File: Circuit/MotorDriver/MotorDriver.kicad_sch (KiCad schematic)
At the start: 28 parts, among them J1 Conn_01x06_Pin, J2 USB_C_Receptacle_USB2.0_16P, SW1 SW_SPDT, SW2 SW_Push_Dual, U1 STM32G473RCTx, U2 CH340E, Y1 24M

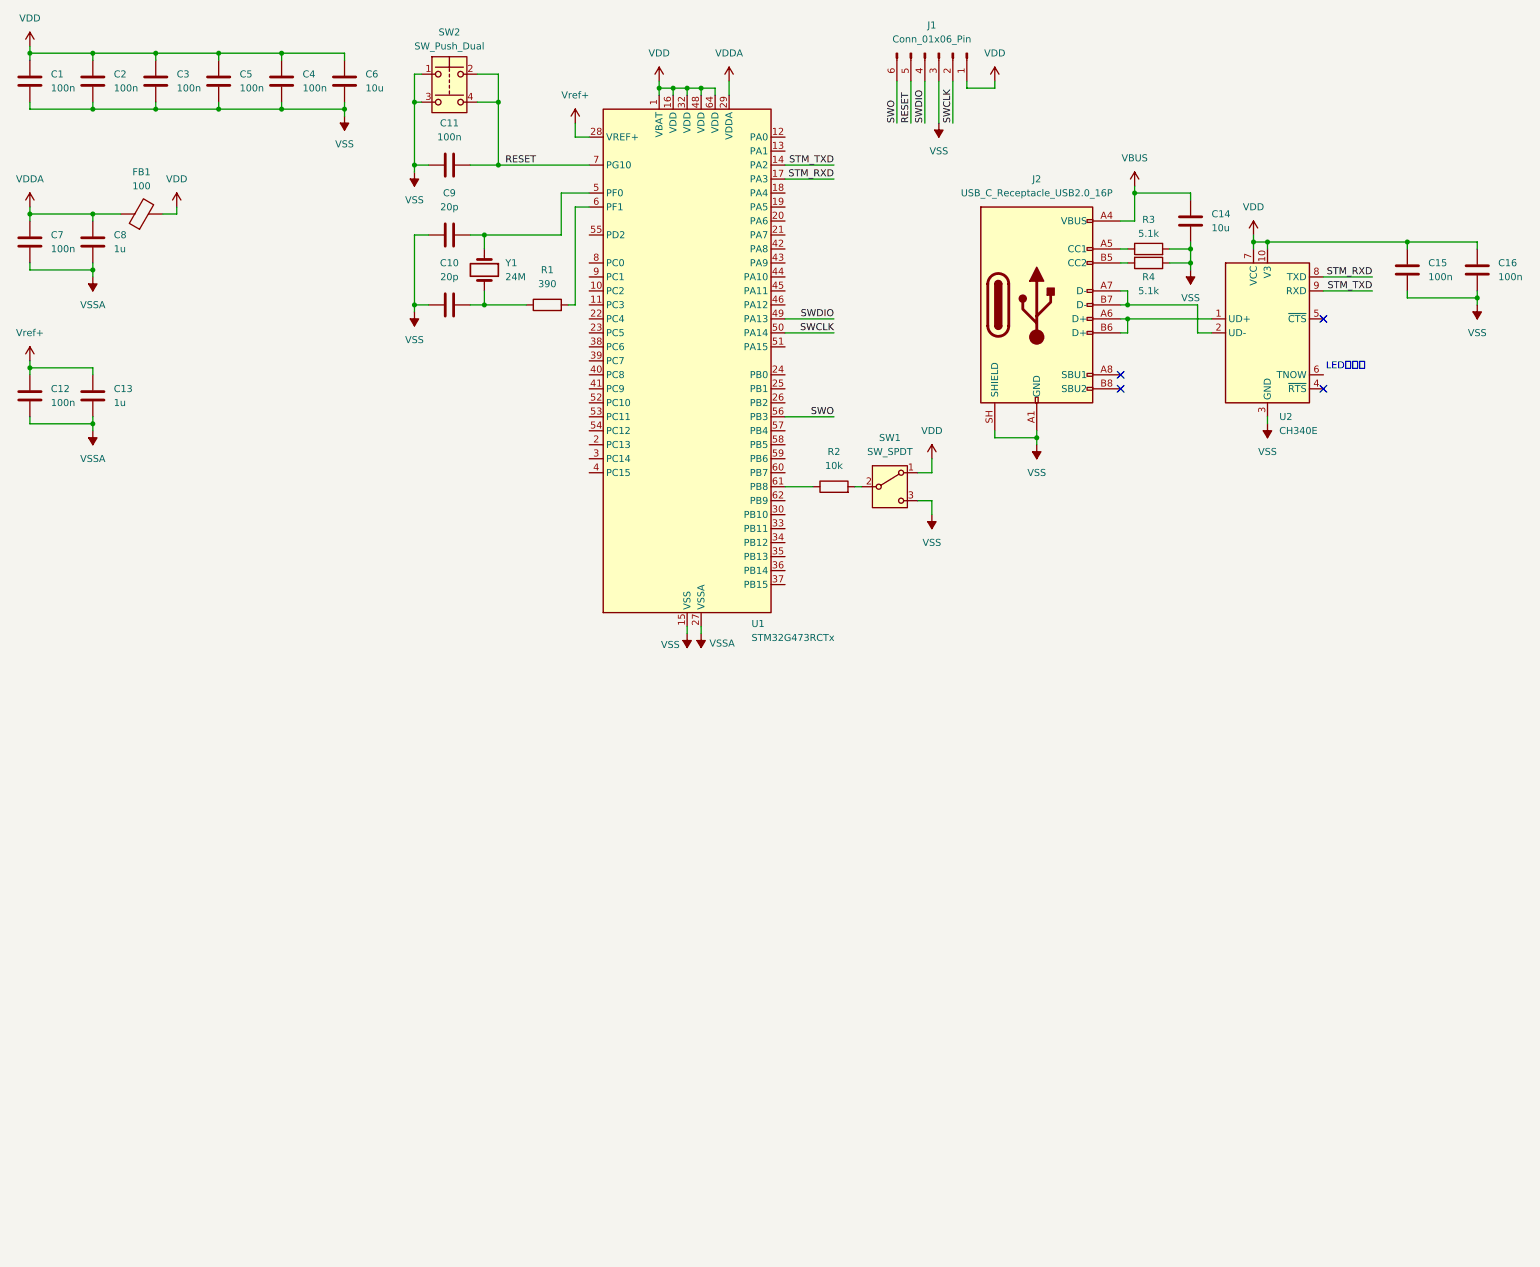
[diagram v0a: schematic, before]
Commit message: ドライバのシンボルを追加
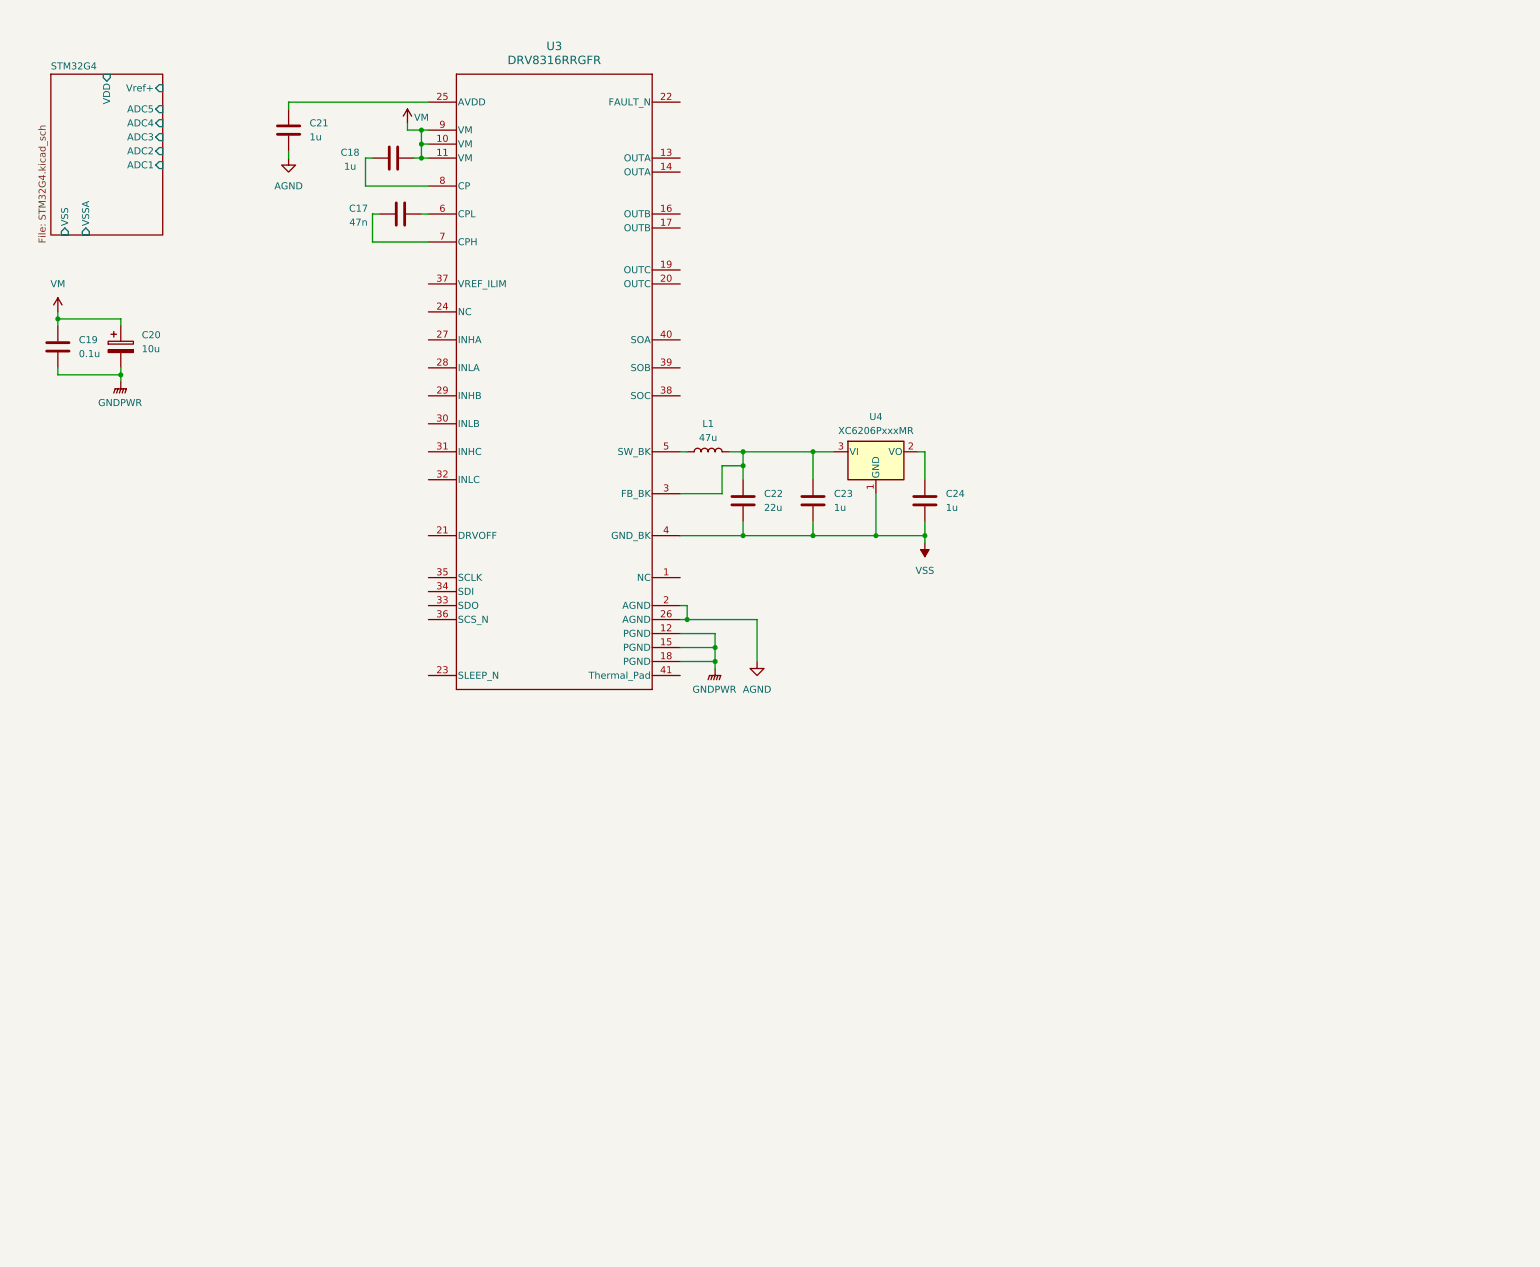
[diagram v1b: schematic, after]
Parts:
- removed C1, C11, C12, C15, C16, C2, C3, C4, C5, C7: 100n, symbol Device:C
- removed C10, C9: 20p, symbol Device:C
- removed C13, C8: 1u, symbol Device:C
- removed C14, C6: 10u, symbol Device:C
- removed FB1: 100, symbol Device:FerriteBead
- removed J1: Conn_01x06_Pin, symbol Connector:Conn_01x06_Pin
- removed J2: USB_C_Receptacle_USB2.0_16P, symbol Connector:USB_C_Receptacle_USB2.0_16P
- removed R1: 390, symbol Device:R
- removed R2: 10k, symbol Device:R
- removed R3, R4: 5.1k, symbol Device:R
- removed SW1: SW_SPDT, symbol Switch:SW_SPDT
- removed SW2: SW_Push_Dual, symbol Switch:SW_Push_Dual
- removed U1: STM32G473RCTx, Package_QFP:LQFP-64_10x10mm_P0.5mm, symbol MCU_ST_STM32G4:STM32G473RCTx
- removed U2: CH340E, Package_SO:MSOP-10_3x3mm_P0.5mm, symbol Interface_USB:CH340E
- removed Y1: 24M, symbol Device:Crystal
- added C17: 47n, symbol Device:C
- added C18, C21, C23, C24: 1u, symbol Device:C
- added C19: 0.1u, symbol Device:C
- added C20: 10u, symbol Device:C_Polarized
- added C22: 22u, symbol Device:C
- added L1: 47u, symbol Device:L
- added U3: DRV8316RRGFR, RGF0040E-IPC_A, symbol OU_power:DRV8316RRGFR
- added U4: XC6206PxxxMR, Package_TO_SOT_SMD:SOT-23-3, symbol Regulator_Linear:XC6206PxxxMR
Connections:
- net VSS: now also C22.2, C23.2, C24.2, U3.4 (GND_BK), U4.1 (GND)
- new net: C22.1, C23.1, L1.2, U3.3 (FB_BK), U4.3 (VI)
- new net: C24.1, U4.2 (VO)
- new net: L1.1, U3.5 (SW_BK)
- new net: C17.1, U3.6 (CPL)
- new net: C17.2, U3.7 (CPH)
- new net: C21.1, U3.25 (AVDD)
- new net: C18.1, U3.8 (CP)
- new net AGND: C21.2, U3.2 (AGND), U3.26 (AGND)
- new net GNDPWR: C19.2, C20.2, U3.12 (PGND), U3.15 (PGND), U3.18 (PGND)
- new net VM: C18.2, C19.1, C20.1, U3.10 (VM), U3.11 (VM), U3.9 (VM)
- no-connect marks 4 -> 0
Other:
- added sheet STM32G4 (STM32G4.kicad_sch)
- note removed: "LEDを接続"

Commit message: PWMとADCの配線等
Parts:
- added C25, C26: 30p, symbol Device:C
- added D1: BZT52C3V3, symbol Device:D_Zener
- added J3: Conn_01x03_Pin, symbol Connector:Conn_01x03_Pin
- added R5: 47k, symbol Device:R
- added R6: 5.1k, symbol Device:R
- added R7, R8: 1k, symbol Device:R
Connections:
- net VSS is gone; now on net AGND: C22.2, C23.2, C24.2, U3.4 (GND_BK), U4.1 (GND)
- net AGND: now also U3.41 (Thermal_Pad), C25.2, C26.2, D1.2 (A)
- net STM32G4/ADC1: now also C25.1, R7.1
- net STM32G4/ADC2: now also C26.1, R8.1
- net VM: now also R5.1
- net VDD: now reaches C24.1, U4.2 (VO)
- net VDD: now also R6.2
- net at U3.13 (OUTA): now also U3.14 (OUTA), J3.1 (Pin_1)
- net at U3.16 (OUTB): now also U3.17 (OUTB), J3.2 (Pin_2)
- net at U3.19 (OUTC): now also U3.20 (OUTC), J3.3 (Pin_3)
- net at U3.22 (FAULT_N): now also R6.1
- net at U3.23 (SLEEP_N): now also D1.1 (K), R5.2
- net STM32G4/PWM1: now reaches U3.27 (INHA)
- net STM32G4/PWM4: now reaches U3.28 (INLA)
- net STM32G4/PWM2: now reaches U3.29 (INHB)
- net STM32G4/PWM5: now reaches U3.30 (INLB)
- net STM32G4/PWM3: now reaches U3.31 (INHC)
- net STM32G4/PWM6: now reaches U3.32 (INLC)
- net Vref+: now reaches U3.37 (VREF_ILIM)
- net at U3.39 (SOB): now also R8.2
- net at U3.40 (SOA): now also R7.2
- no-connect marks 0 -> 3
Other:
- sheet STM32G4 ports: added PWM1, PWM2, PWM3, PWM4, PWM5, PWM6; removed none
- moved on the sheet: C17, C18, C19, C20, C21, C22, C23, C24, L1, U3, U4

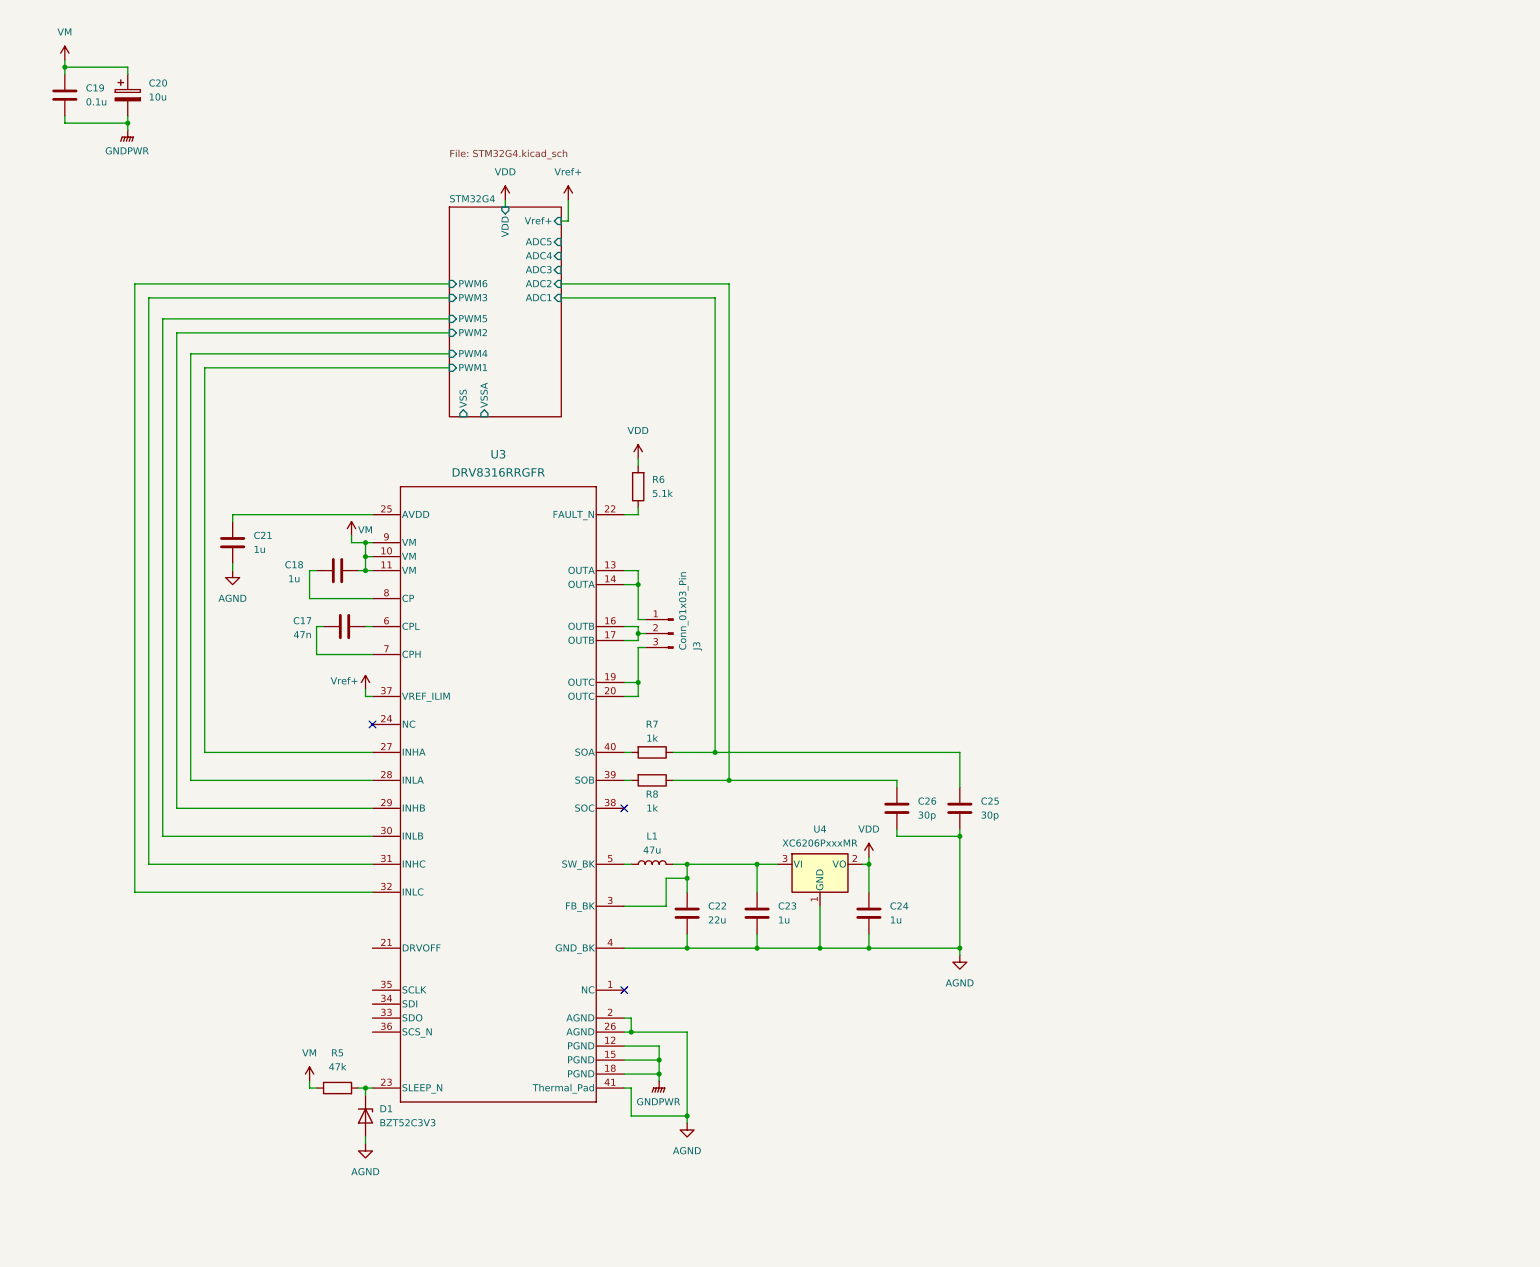
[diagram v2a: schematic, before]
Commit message: エンコーダの配線等
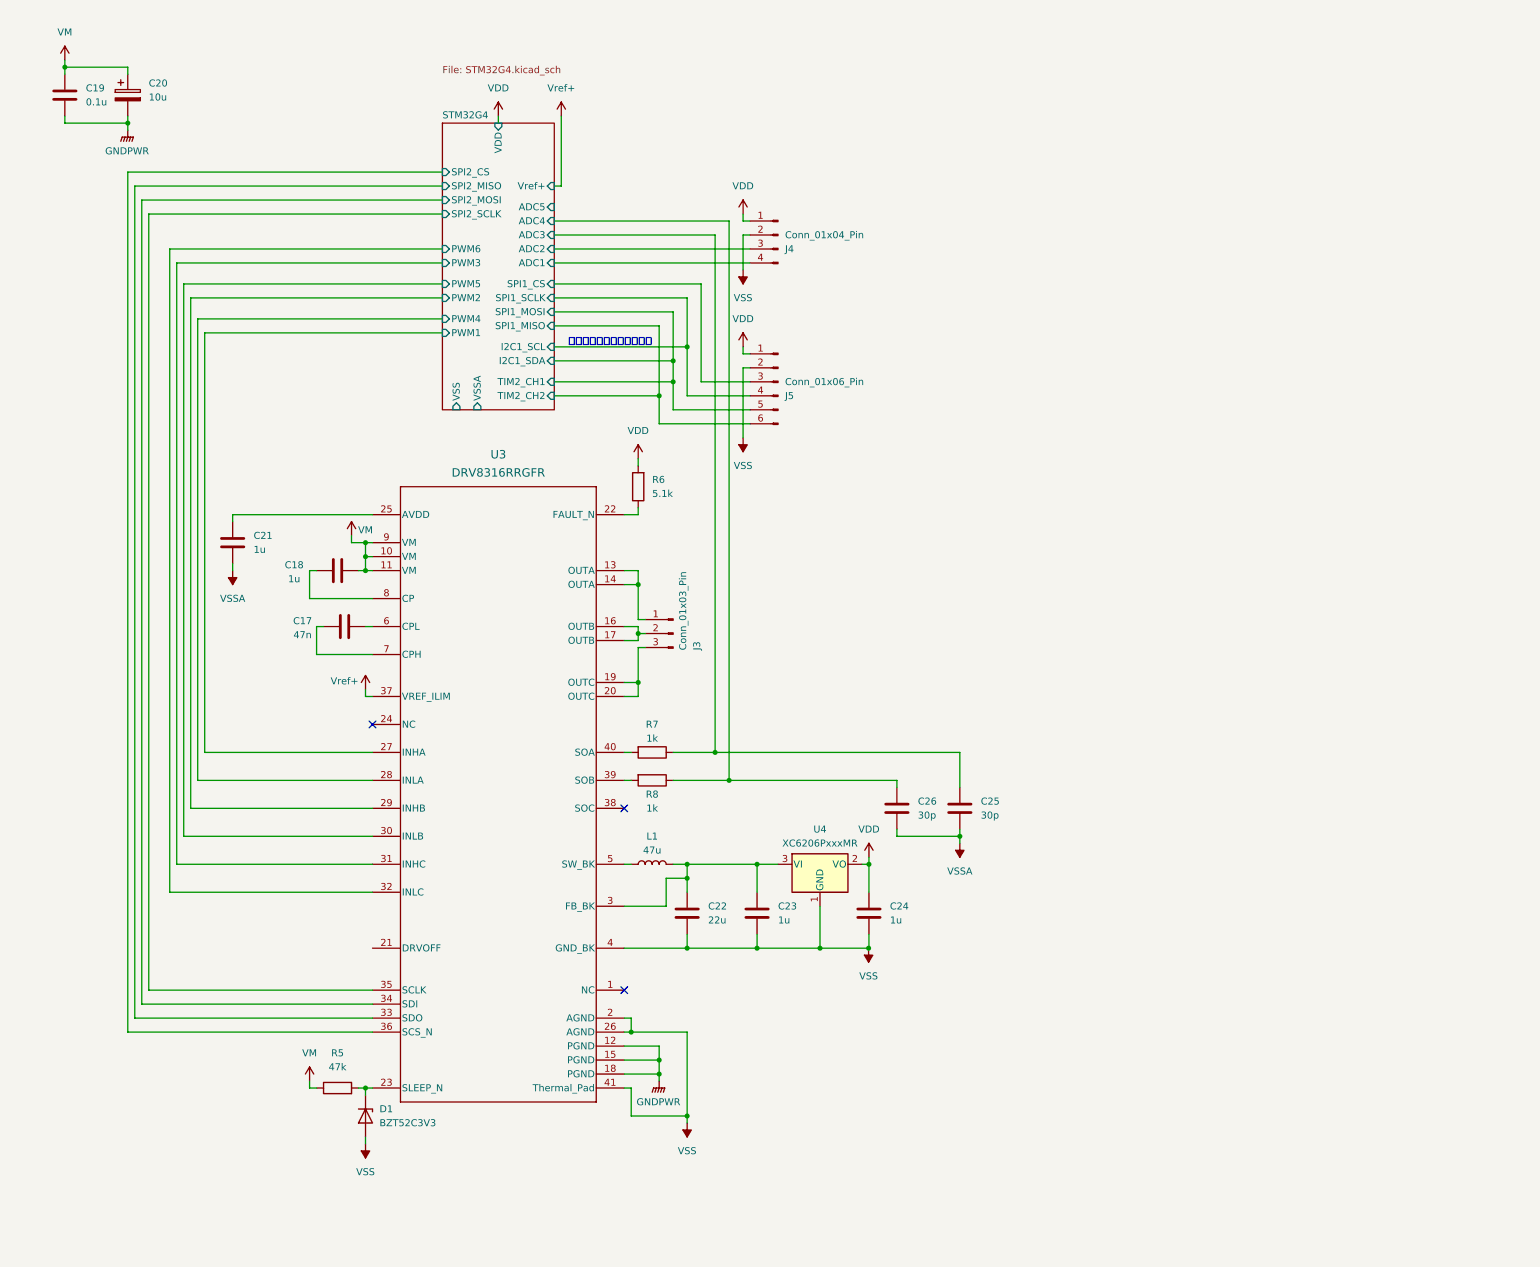
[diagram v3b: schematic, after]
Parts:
- added J4: Conn_01x04_Pin, symbol Connector:Conn_01x04_Pin
- added J5: Conn_01x06_Pin, symbol Connector:Conn_01x06_Pin
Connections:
- net STM32G4/ADC1: now also J4.4 (Pin_4); no longer C25.1, R7.1
- net STM32G4/ADC2: now also J4.3 (Pin_3); no longer C26.1, R8.1
- net STM32G4/ADC3: now also C25.1, R7.1
- net STM32G4/ADC4: now also C26.1, R8.1
- net VDD: now also J4.1 (Pin_1), J5.1 (Pin_1)
- net STM32G4/SPI2_MISO: now reaches U3.33 (SDO)
- net STM32G4/SPI2_MOSI: now reaches U3.34 (SDI)
- net STM32G4/SPI2_SCLK: now reaches U3.35 (SCLK)
- net STM32G4/SPI2_CS: now reaches U3.36 (SCS_N)
- net AGND renamed VSS
- net VSS: now also J4.2 (Pin_2), J5.2 (Pin_2); no longer C21.2, C25.2, C26.2
- new net STM32G4/I2C1_SCL: J5.4 (Pin_4)
- new net STM32G4/I2C1_SDA: J5.5 (Pin_5)
- new net STM32G4/SPI1_CS: J5.3 (Pin_3)
- new net STM32G4/SPI1_MISO: J5.6 (Pin_6)
- new net VSSA: C21.2, C25.2, C26.2
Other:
- sheet STM32G4 ports: added I2C1_SCL, I2C1_SDA, SPI1_CS, SPI1_MISO, SPI1_MOSI, SPI1_SCLK, SPI2_CS, SPI2_MISO, SPI2_MOSI, SPI2_SCLK, TIM2_CH1, TIM2_CH2; removed none
- note added: "プルアップ抵抗どうする？"
